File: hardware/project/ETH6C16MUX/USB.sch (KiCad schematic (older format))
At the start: 15 parts, among them J501 105133-0001, U501 FT230XQ, U502 824011

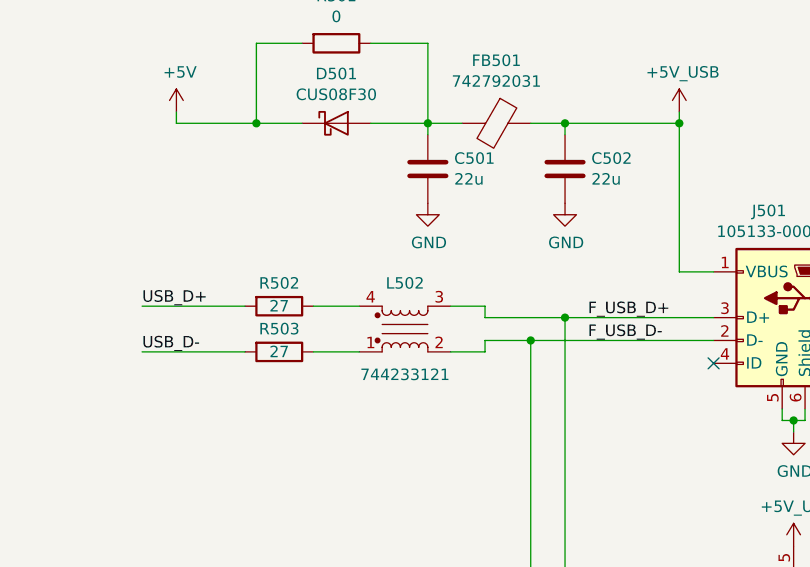
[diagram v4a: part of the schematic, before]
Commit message: PCB layout, board to board connector changed.
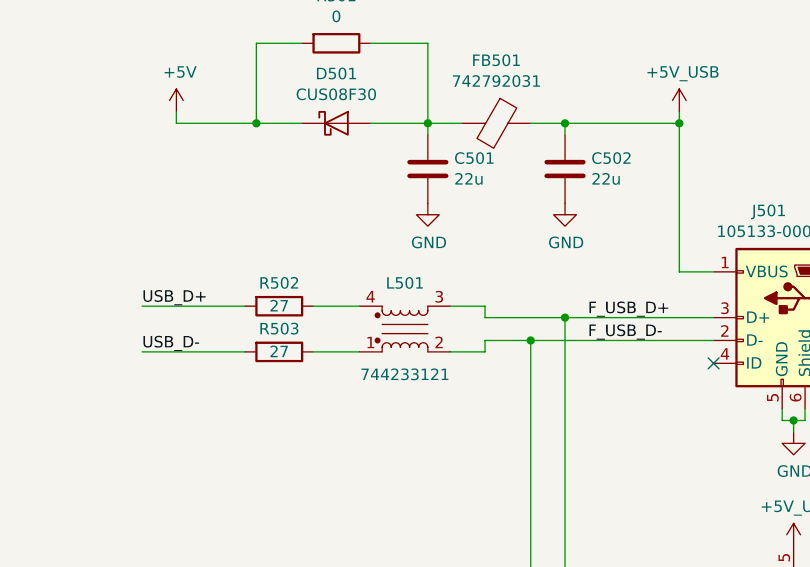
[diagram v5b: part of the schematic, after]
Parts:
- renumbered L502 to L501
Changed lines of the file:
@@
 $Descr A4 11693 8268
 encoding utf-8
-Sheet 5 9
+Sheet 5 8
 Title "USB"
 Date ""
@@
 	7700 3450 7700 3500
 $Comp
-L ETH6C16MUX:744233121 L502
+L ETH6C16MUX:744233121 L501
 U 1 1 5D613F1C
 P 7350 3400
-F 0 "L502" H 7350 3600 50  0000 C CNN
+F 0 "L501" H 7350 3600 50  0000 C CNN
 F 1 "744233121" H 7350 3200 50  0000 C CNN
 F 2 "ETH6C16MXU:744233121" H 7350 3400 50  0001 C CNN
@@
 $EndComp
 $Comp
-L power:GND #PWR0137
+L power:GND #PWR0507
 U 1 1 61DC20ED
 P 9050 3850
-F 0 "#PWR0137" H 9050 3600 50  0001 C CNN
+F 0 "#PWR0507" H 9050 3600 50  0001 C CNN
 F 1 "GND" H 9055 3677 50  0000 C CNN
 F 2 "" H 9050 3850 50  0001 C CNN
@@
 $EndComp
 $Comp
-L power:GND #PWR0138
+L power:GND #PWR0511
 U 1 1 61DC2D16
 P 9050 5000
-F 0 "#PWR0138" H 9050 4750 50  0001 C CNN
+F 0 "#PWR0511" H 9050 4750 50  0001 C CNN
 F 1 "GND" H 9055 4827 50  0000 C CNN
 F 2 "" H 9050 5000 50  0001 C CNN
@@
 $EndComp
 $Comp
-L power:GND #PWR0139
+L power:GND #PWR0503
 U 1 1 61DC3367
 P 7450 2850
-F 0 "#PWR0139" H 7450 2600 50  0001 C CNN
+F 0 "#PWR0503" H 7450 2600 50  0001 C CNN
 F 1 "GND" H 7455 2677 50  0000 C CNN
 F 2 "" H 7450 2850 50  0001 C CNN
@@
 $EndComp
 $Comp
-L power:GND #PWR0140
+L power:GND #PWR0504
 U 1 1 61DC47AE
 P 8050 2850
-F 0 "#PWR0140" H 8050 2600 50  0001 C CNN
+F 0 "#PWR0504" H 8050 2600 50  0001 C CNN
 F 1 "GND" H 8055 2677 50  0000 C CNN
 F 2 "" H 8050 2850 50  0001 C CNN

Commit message: PCB layout, deleted USB.
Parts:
- R501: footprint Resistor_SMD:R_0612_1632Metric_Pad1.18x3.40mm_HandSolder -> Resistor_SMD:R_0603_1608Metric_Pad1.05x0.95mm_HandSolder
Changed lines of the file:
@@
 F 0 "R501" V 6843 2150 50  0000 C CNN
 F 1 "0" V 6934 2150 50  0000 C CNN
-F 2 "Resistor_SMD:R_0612_1632Metric_Pad1.18x3.40mm_HandSolder" V 6980 2150 50  0001 C CNN
+F 2 "Resistor_SMD:R_0603_1608Metric_Pad1.05x0.95mm_HandSolder" V 6980 2150 50  0001 C CNN
 F 3 "~" H 7050 2150 50  0001 C CNN
 	1    7050 2150
